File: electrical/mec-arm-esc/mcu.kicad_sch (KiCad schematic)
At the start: 15 parts, among them SW1 SH-1808SN-250GF, SW2 SH-1808SN-250GF, U2 STM32G474RET3

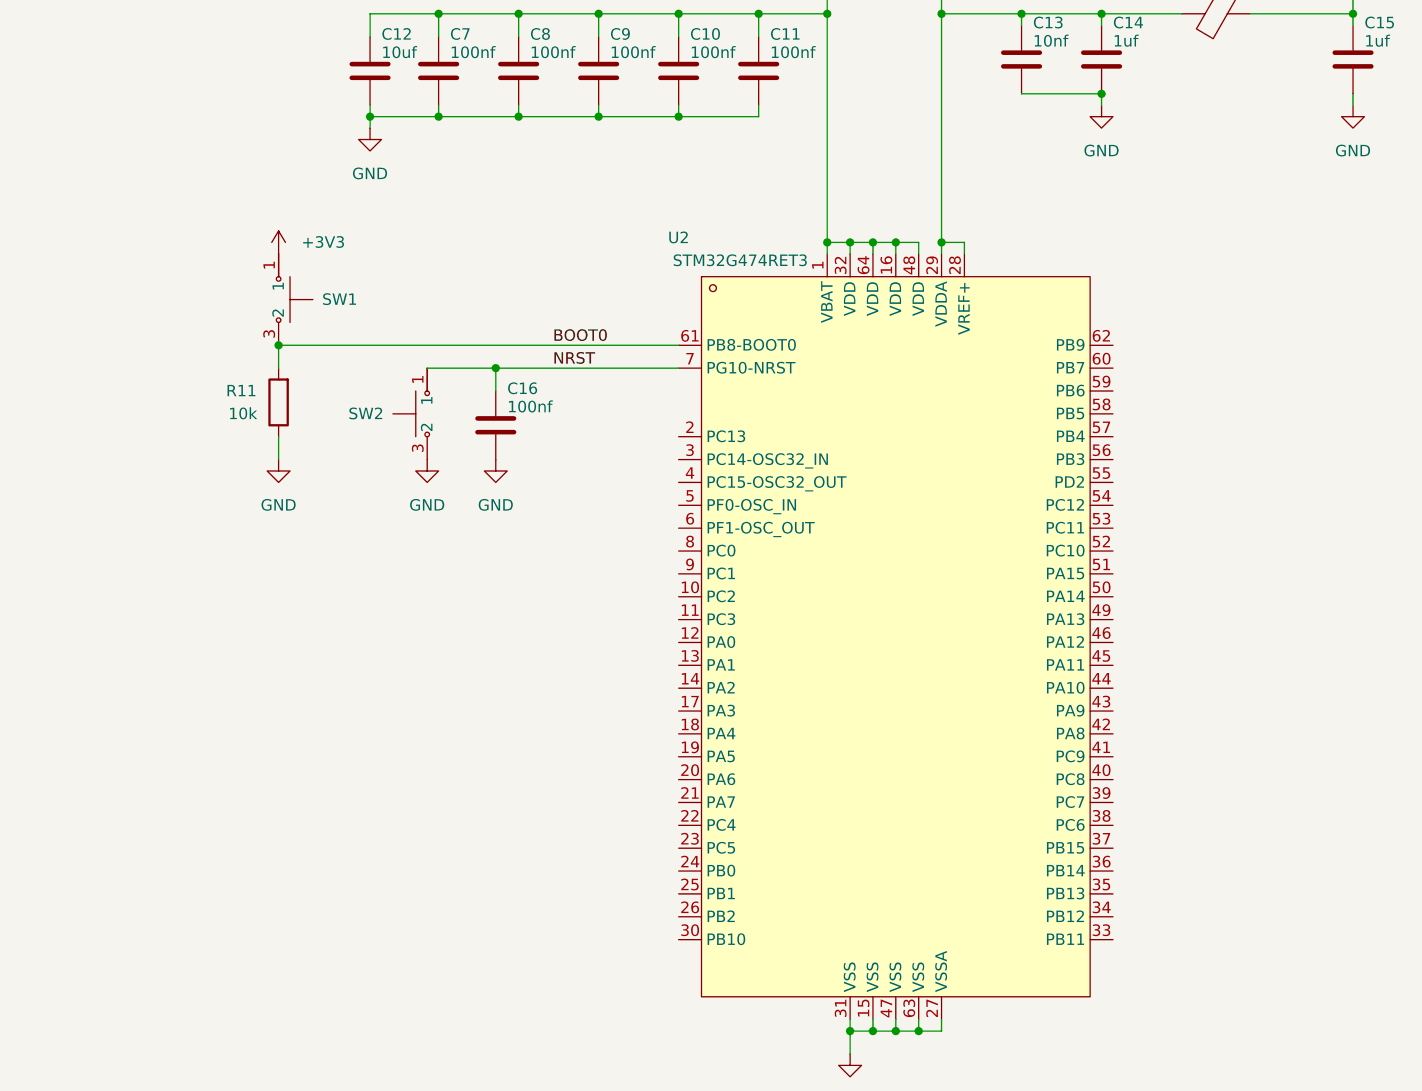
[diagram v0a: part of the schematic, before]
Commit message: Finished Bare MCU + Oscillator, added prelim powerstage additions
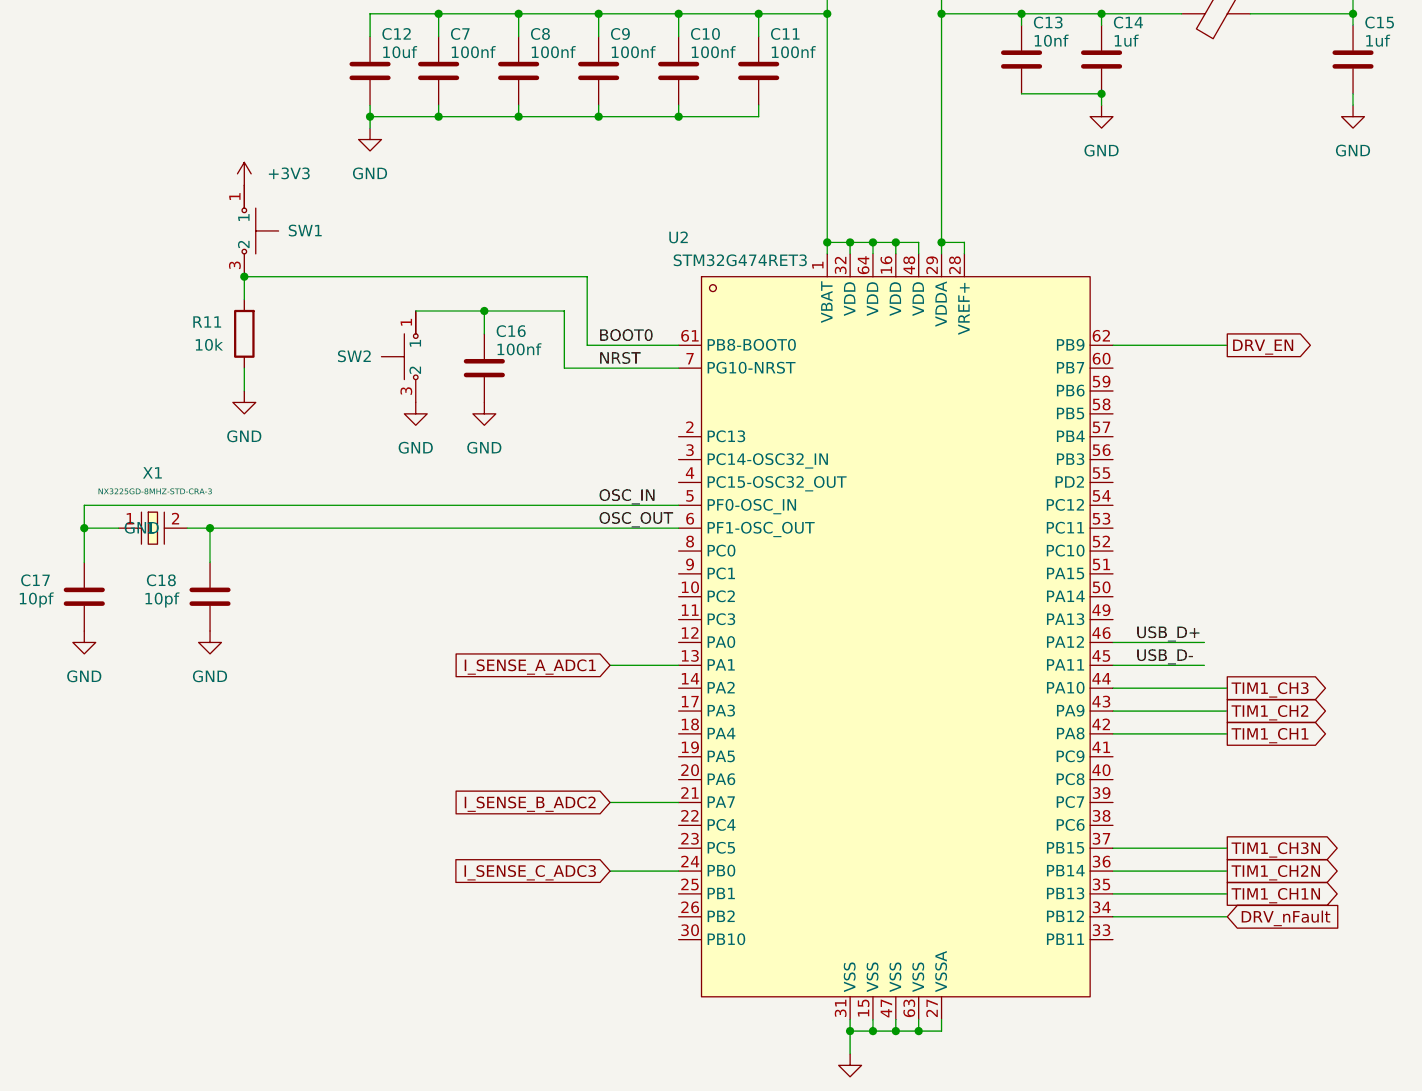
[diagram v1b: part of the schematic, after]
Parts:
- added C17, C18: 10pf, symbol Device:C
- added X1: NX3225GD-8MHZ-STD-CRA-3, EasyEDA:OSC-SMD_2P-L3.2-W2.5, symbol core:NX3225GD-8MHZ-STD-CRA-3
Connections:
- net GND: now also C17.2, C18.2
- net I_SENSE_A_ADC1: now reaches U2.13 (PA1)
- net I_SENSE_B_ADC2: now reaches U2.21 (PA7)
- net I_SENSE_C_ADC3: now reaches U2.24 (PB0)
- net DRV_nFault: now reaches U2.34 (PB12)
- net TIM1_CH1N: now reaches U2.35 (PB13)
- net TIM1_CH2N: now reaches U2.36 (PB14)
- net TIM1_CH3N: now reaches U2.37 (PB15)
- net TIM1_CH1: now reaches U2.42 (PA8)
- net TIM1_CH2: now reaches U2.43 (PA9)
- net TIM1_CH3: now reaches U2.44 (PA10)
- net USB_D-: now reaches U2.45 (PA11)
- net USB_D+: now reaches U2.46 (PA12)
- net OSC_IN: now reaches U2.5 (PF0-OSC_IN)
- net OSC_IN: now also C17.1, X1.1
- net OSC_OUT: now reaches U2.6 (PF1-OSC_OUT)
- net OSC_OUT: now also C18.1, X1.2 (GND)
- net DRV_EN: now reaches U2.62 (PB9)
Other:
- moved on the sheet: C16, R11, SW1, SW2

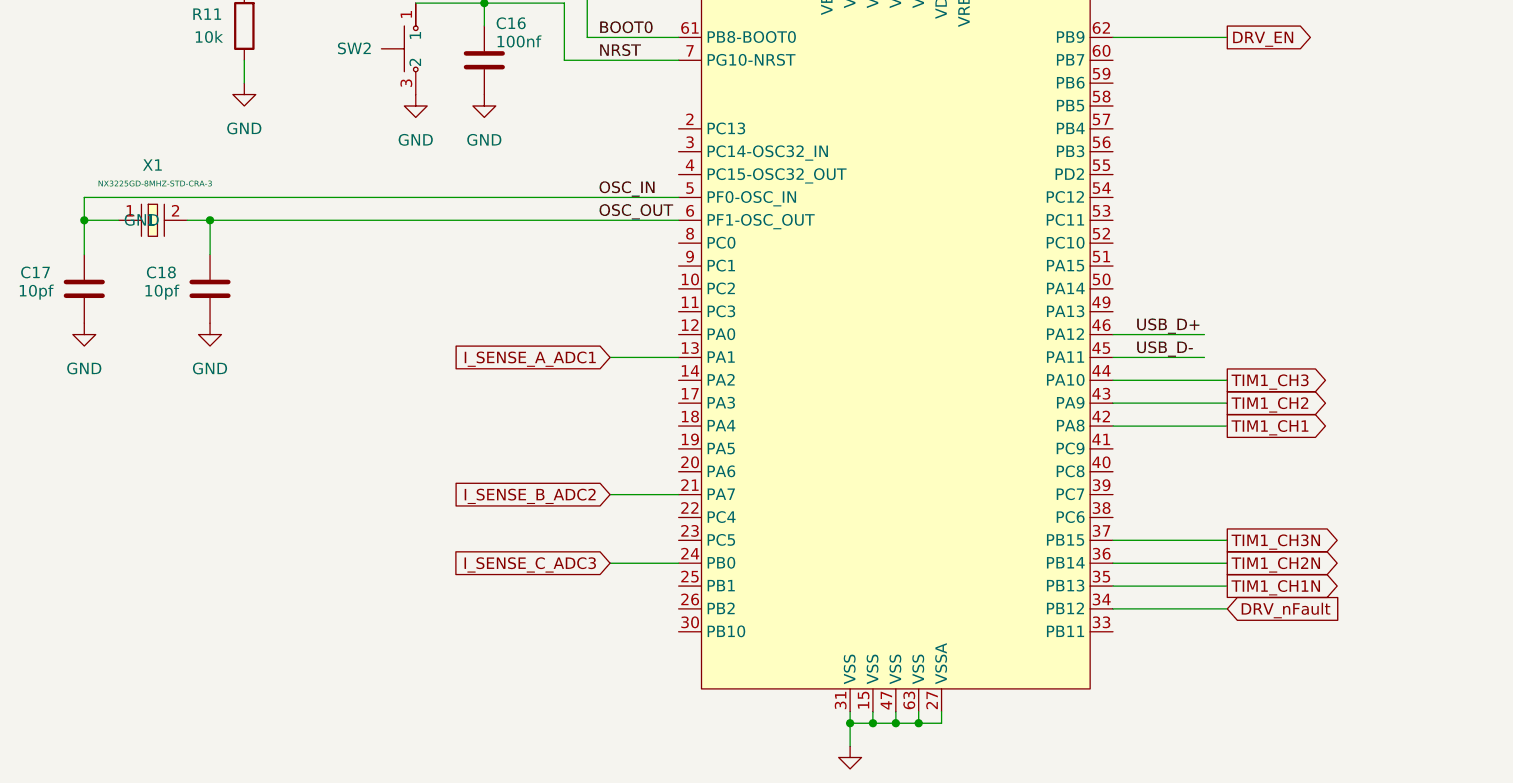
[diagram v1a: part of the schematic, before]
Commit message: Completed inverter, started calculation for input power
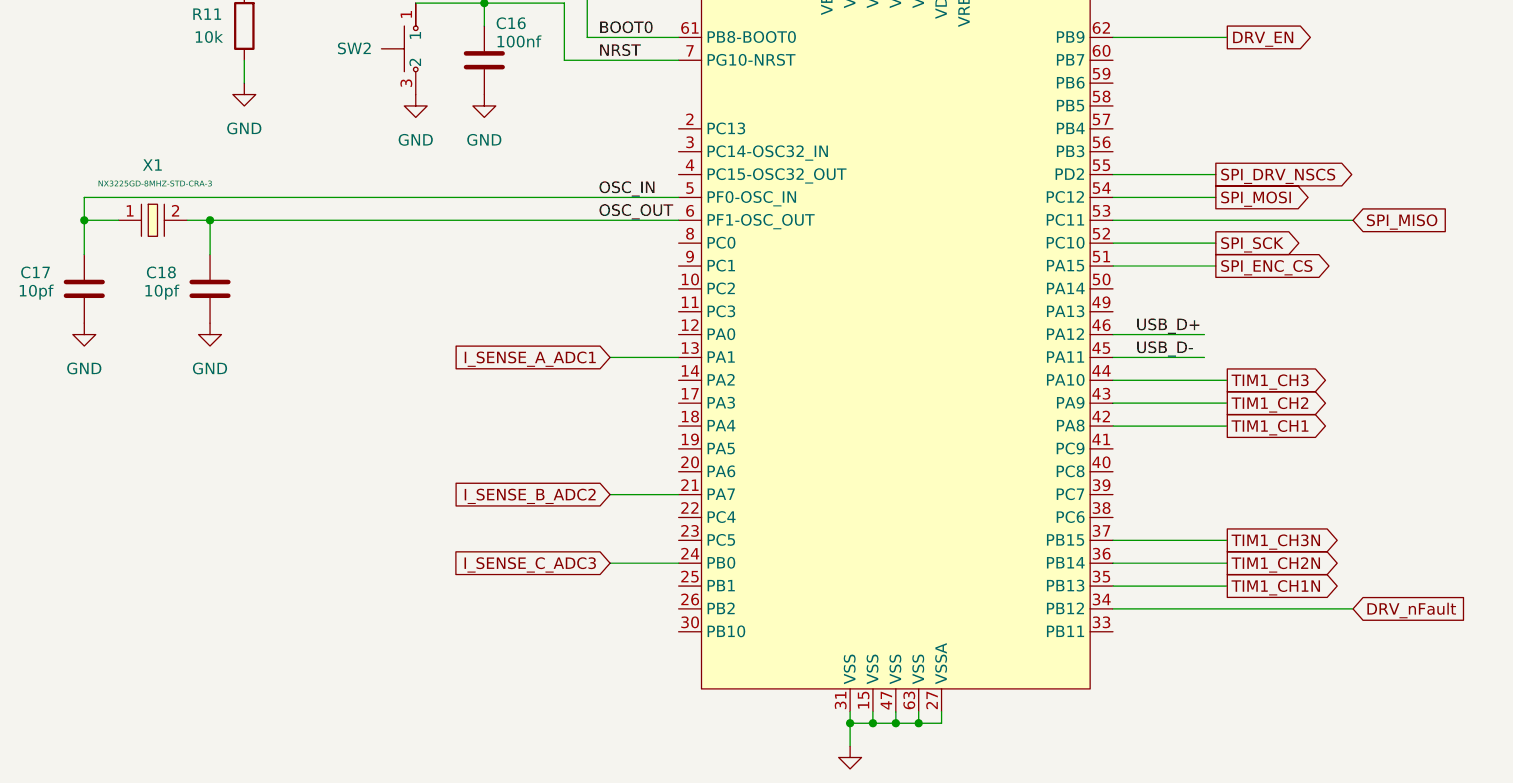
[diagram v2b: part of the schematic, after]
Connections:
- net SPI_ENC_CS: now reaches U2.51 (PA15)
- net SPI_SCK: now reaches U2.52 (PC10)
- net SPI_MISO: now reaches U2.53 (PC11)
- net SPI_MOSI: now reaches U2.54 (PC12)
- net SPI_DRV_NSCS: now reaches U2.55 (PD2)
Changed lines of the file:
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@@
 	(wire
 		(pts
-			(xy 227.33 153.67) (xy 240.03 153.67)
+			(xy 227.33 153.67) (xy 254 153.67)
 		)
 		(stroke
@@
 	(wire
 		(pts
+			(xy 227.33 105.41) (xy 238.76 105.41)
+		)
+		(stroke
+			(width 0)
+			(type default)
+		)
+	)
+	(wire
+		(pts
 			(xy 198.12 166.37) (xy 198.12 168.91)
 		)
@@
 	(wire
 		(pts
+			(xy 227.33 107.95) (xy 238.76 107.95)
+		)
+		(stroke
+			(width 0)
+			(type default)
+		)
+	)
+	(wire
+		(pts
 			(xy 198.12 80.01) (xy 198.12 78.74)
 		)
@@
 	(wire
 		(pts
+			(xy 227.33 110.49) (xy 254 110.49)
+		)
+		(stroke
+			(width 0)
+			(type default)
+		)
+	)
+	(wire
+		(pts
 			(xy 168.91 82.55) (xy 168.91 90.17)
 		)
@@
 	(wire
 		(pts
+			(xy 227.33 113.03) (xy 238.76 113.03)
+		)
+		(stroke
+			(width 0)
+			(type default)
+		)
+	)
+	(wire
+		(pts
 			(xy 226.06 62.23) (xy 226.06 63.5)
 		)
@@
 	(wire
 		(pts
+			(xy 227.33 115.57) (xy 238.76 115.57)
+		)
+		(stroke
+			(width 0)
+			(type default)
+		)
+	)
+	(wire
+		(pts
 			(xy 130.81 82.55) (xy 168.91 82.55)
 		)
@@
 		)
 	)
+	(global_label "SPI_MOSI"
+		(shape output)
+		(at 238.76 107.95 0)
+		(fields_autoplaced yes)
+		(effects
+			(font
+				(size 1.27 1.27)
+			)
+			(justify left)
+		)
+		(property "Intersheetrefs" "${INTERSHEET_REFS}"
+			(at 250.3933 107.95 0)
+			(hide yes)
+			(show_name no)
+			(do_not_autoplace no)
+			(effects
+				(font
+					(size 1.27 1.27)
+				)
+				(justify left)
+			)
+		)
+	)
 	(global_label "TIM1_CH3"
 		(shape output)
@@
 	(global_label "DRV_nFault"
 		(shape input)
-		(at 240.03 153.67 0)
+		(at 254 153.67 0)
 		(fields_autoplaced yes)
 		(effects
@@
 		)
 		(property "Intersheetrefs" "${INTERSHEET_REFS}"
-			(at 254.2031 153.67 0)
+			(at 268.1731 153.67 0)
 			(hide yes)
 			(show_name no)
@@
 		)
 	)
+	(global_label "SPI_SCK"
+		(shape output)
+		(at 238.76 113.03 0)
+		(fields_autoplaced yes)
+		(effects
+			(font
+				(size 1.27 1.27)
+			)
+			(justify left)
+		)
+		(property "Intersheetrefs" "${INTERSHEET_REFS}"
+			(at 249.5466 113.03 0)
+			(hide yes)
+			(show_name no)
+			(do_not_autoplace no)
+			(effects
+				(font
+					(size 1.27 1.27)
+				)
+				(justify left)
+			)
+		)
+	)
 	(global_label "TIM1_CH2"
 		(shape output)
@@
 		)
 	)
+	(global_label "SPI_ENC_CS"
+		(shape output)
+		(at 238.76 115.57 0)
+		(fields_autoplaced yes)
+		(effects
+			(font
+				(size 1.27 1.27)
+			)
+			(justify left)
+		)
+		(property "Intersheetrefs" "${INTERSHEET_REFS}"
+			(at 252.9937 115.57 0)
+			(hide yes)
+			(show_name no)
+			(do_not_autoplace no)
+			(effects
+				(font
+					(size 1.27 1.27)
+				)
+				(justify left)
+			)
+		)
+	)
+	(global_label "SPI_MISO"
+		(shape input)
+		(at 254 110.49 0)
+		(fields_autoplaced yes)
+		(effects
+			(font
+				(size 1.27 1.27)
+			)
+			(justify left)
+		)
+		(property "Intersheetrefs" "${INTERSHEET_REFS}"
+			(at 265.6333 110.49 0)
+			(hide yes)
+			(show_name no)
+			(do_not_autoplace no)
+			(effects
+				(font
+					(size 1.27 1.27)
+				)
+				(justify left)
+			)
+		)
+	)
 	(global_label "I_SENSE_A_ADC1"
 		(shape input)
@@
 		)
 	)
+	(global_label "SPI_DRV_NSCS"
+		(shape output)
+		(at 238.76 105.41 0)
+		(fields_autoplaced yes)
+		(effects
+			(font
+				(size 1.27 1.27)
+			)
+			(justify left)
+		)
+		(property "Intersheetrefs" "${INTERSHEET_REFS}"
+			(at 255.4128 105.41 0)
+			(hide yes)
+			(show_name no)
+			(do_not_autoplace no)
+			(effects
+				(font
+					(size 1.27 1.27)
+				)
+				(justify left)
+			)
+		)
+	)
 	(global_label "DRV_EN"
 		(shape output)
@@
 			)
 		)
-		(property "Description" ""
+		(property "Description" "8MHzz Oscillator"
 			(at 120.65 110.49 0)
 			(hide yes)
